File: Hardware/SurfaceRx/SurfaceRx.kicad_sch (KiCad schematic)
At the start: 27 parts, among them IC1 SC189ZSKTRT, J1 Conn_01x03, J2 Conn_01x03, J3 Conn_01x03, J4 Conn_01x03, J5 Conn_01x03, J6 Conn_01x03, J7 Conn_01x05, J8 Conn_01x03, J9 Conn_01x05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

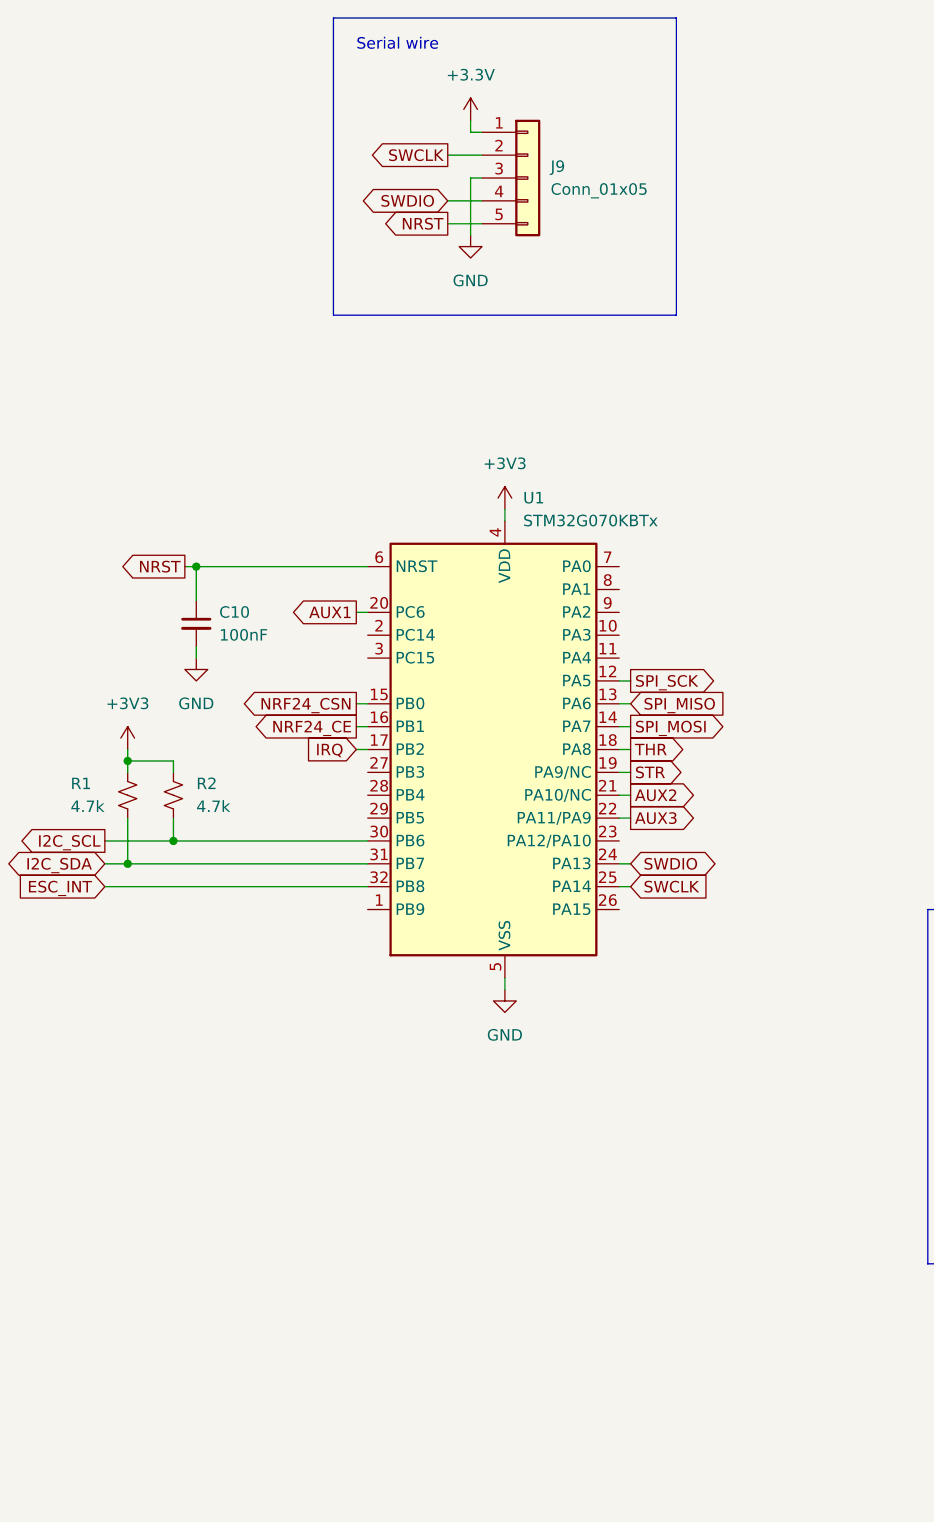
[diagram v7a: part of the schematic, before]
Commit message: Reverted debug header to pads. Added status LED
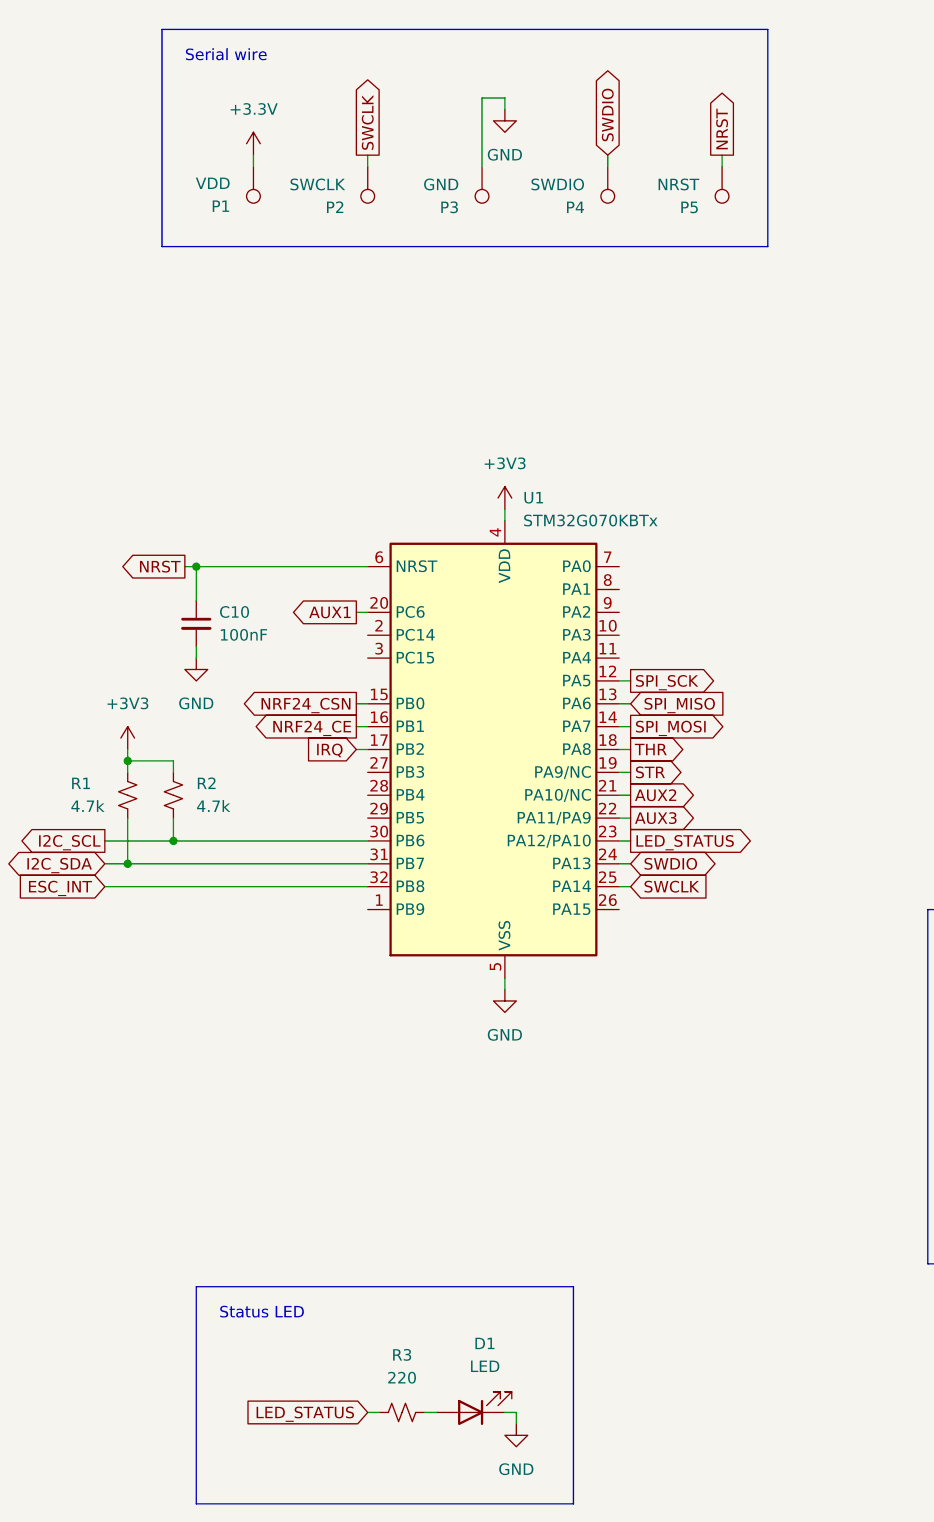
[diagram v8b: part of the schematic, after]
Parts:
- removed J9: Conn_01x05, Connector_PinHeader_2.54mm:PinHeader_1x05_P2.54mm_Vertical, symbol Connector_Generic:Conn_01x05
- added D1: LED, LED_SMD:LED_0603_1608Metric, symbol Device:LED
- added P1: VDD, TestPoint:TestPoint_Pad_D1.5mm, symbol Connector:TestPoint
- added P2: SWCLK, TestPoint:TestPoint_Pad_D1.5mm, symbol Connector:TestPoint
- added P3: GND, TestPoint:TestPoint_Pad_D1.5mm, symbol Connector:TestPoint
- added P4: SWDIO, TestPoint:TestPoint_Pad_D1.5mm, symbol Connector:TestPoint
- added P5: NRST, TestPoint:TestPoint_Pad_D1.5mm, symbol Connector:TestPoint
- added R3: 220, Resistor_SMD:R_0603_1608Metric, symbol Device:R_Small_US
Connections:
- net +3.3V: now also P1.1
- net GND: now also D1.1 (K), P3.1
- net NRST: now also P5.1
- net SWCLK: now also P2.1
- net SWDIO: now also P4.1
- net LED_STATUS: now reaches U1.23 (PA12/PA10)
- net LED_STATUS: now also R3.2
- new net: D1.2 (A), R3.1
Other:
- note added: "Status LED"
